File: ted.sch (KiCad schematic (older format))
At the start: 20 parts, among them Q1 2SC1815, Q2 2SC1815, U1 MOS_7360_TED, Y1 Crystal

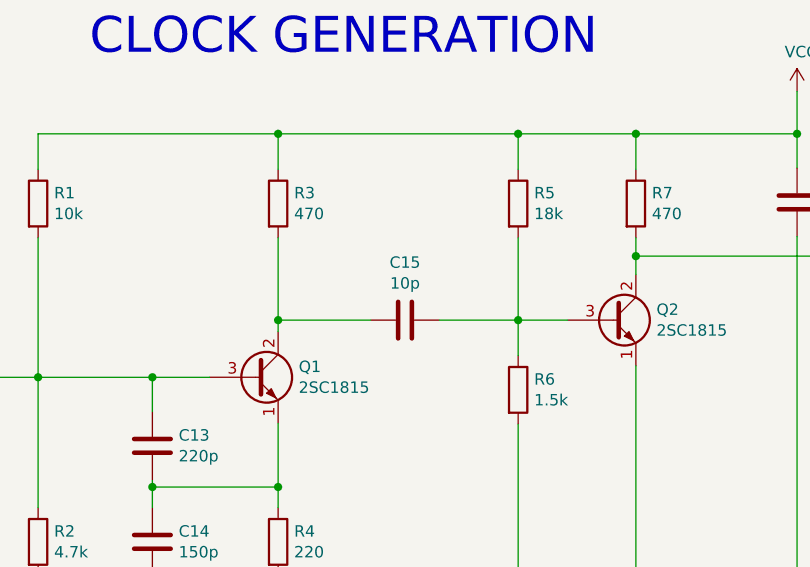
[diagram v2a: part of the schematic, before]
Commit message: C15 -> 10nF
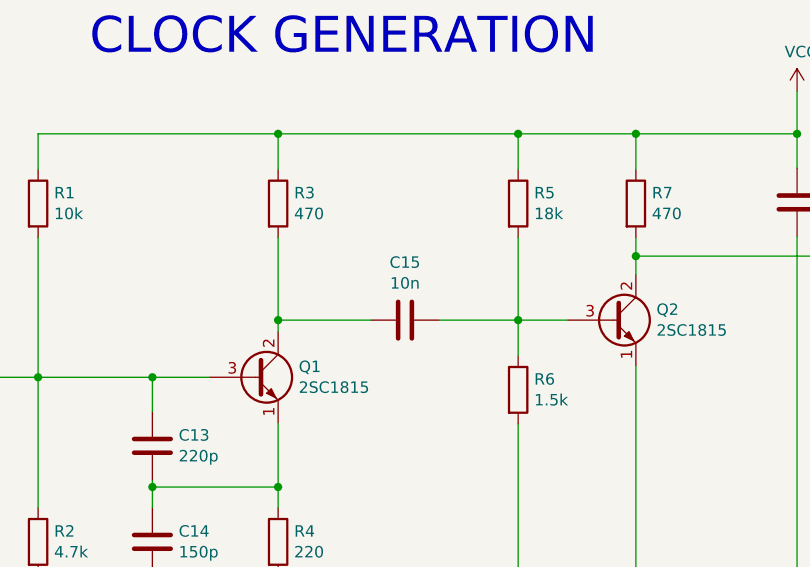
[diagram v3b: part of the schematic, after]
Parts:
- C15: value 10p -> 10n
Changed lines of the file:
@@
 P 3855 3130
 F 0 "C15" V 3603 3130 50  0000 C CNN
-F 1 "10p" V 3694 3130 50  0000 C CNN
+F 1 "10n" V 3694 3130 50  0000 C CNN
 F 2 "Capacitor_THT:C_Disc_D8.0mm_W2.5mm_P5.00mm" H 3893 2980 50  0001 C CNN
 F 3 "~" H 3855 3130 50  0001 C CNN

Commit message: Make most ICs HCT
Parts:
- Q1, Q2: MouserPN (none) -> 610-2SC1815-GR
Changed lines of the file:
@@
 F 2 "Package_TO_SOT_THT:TO-92_Inline_Wide" H 3400 3305 50  0001 L CIN
 F 3 "https://media.digikey.com/pdf/Data%20Sheets/Toshiba%20PDFs/2SC1815.pdf" H 3200 3380 50  0001 L CNN
+F 4 "610-2SC1815-GR" H 3200 3380 50  0001 C CNN "MouserPN"
 	1    3200 3380
 	1    0    0    -1
@@
 F 2 "Package_TO_SOT_THT:TO-92_Inline_Wide" H 4965 3055 50  0001 L CIN
 F 3 "https://media.digikey.com/pdf/Data%20Sheets/Toshiba%20PDFs/2SC1815.pdf" H 4765 3130 50  0001 L CNN
+F 4 "610-2SC1815-GR" H 4765 3130 50  0001 C CNN "MouserPN"
 	1    4765 3130
 	1    0    0    -1

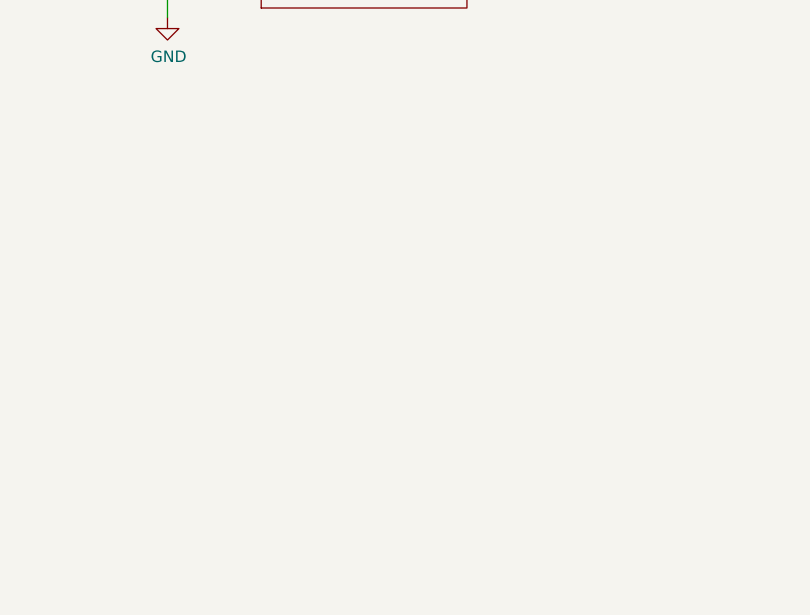
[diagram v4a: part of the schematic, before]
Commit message: Add TED direct audio output header (Experimental)
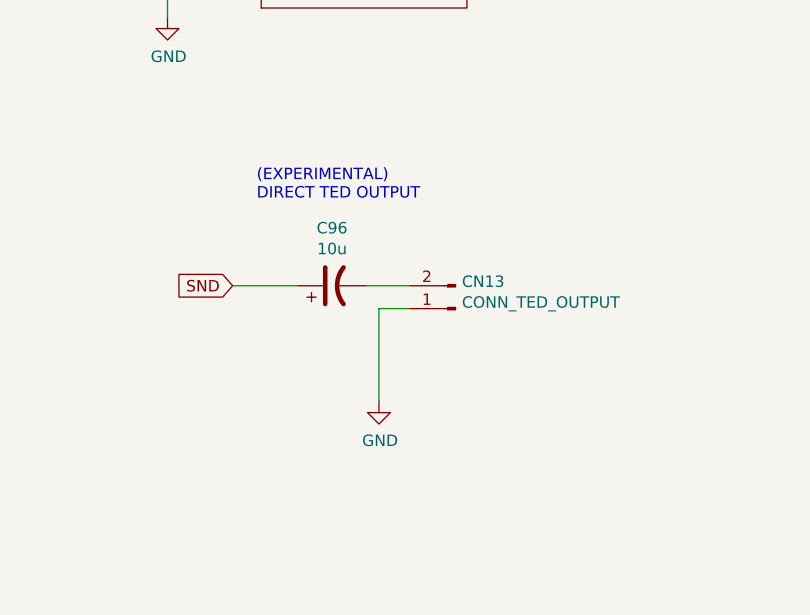
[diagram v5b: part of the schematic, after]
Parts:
- added C96: 10u, Capacitor_THT:CP_Radial_D5.0mm_P2.00mm, symbol Device:CP1
- added CN13: CONN_TED_OUTPUT, Connector_PinHeader_2.54mm:PinHeader_1x02_P2.54mm_Vertical, symbol Connector:Conn_01x02_Male
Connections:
- net GND: now also CN13.1 (Pin_1)
- net SND: now also C96.1
- new net: C96.2, CN13.2 (Pin_2)
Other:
- note added: "(EXPERIMENTAL)\nDIRECT TED OUTPUT"
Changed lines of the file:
@@
 	0    -1   1    0
 $EndComp
+Wire Wire Line
+	8250 5365 8250 5770
+Wire Wire Line
+	8385 5365 8250 5365
+Text Notes 7715 4895 0    50   ~ 0
+(EXPERIMENTAL)\nDIRECT TED OUTPUT
+Wire Wire Line
+	8195 5265 8385 5265
+$Comp
+L Connector:Conn_01x02_Male CN?
+U 1 1 64CE27EC
+P 8585 5365
+AR Path="/64A6E6F3/64CE27EC" Ref="CN?"  Part="1"
+AR Path="/5DE044CB/64CE27EC" Ref="CN13"  Part="1"
+F 0 "CN13" H 8557 5247 50  0000 R CNN
+F 1 "CONN_TED_OUTPUT" H 8557 5338 50  0000 R CNN
+F 2 "Connector_PinHeader_2.54mm:PinHeader_1x02_P2.54mm_Vertical" H 8585 5365 50  0001 C CNN
+F 3 "~" H 8585 5365 50  0001 C CNN
+	1    8585 5365
+	-1   0    0    1
+$EndComp
+$Comp
+L Device:CP1 C?
+U 1 1 64CE27F4
+P 8045 5265
+AR Path="/64A6E6F3/64CE27F4" Ref="C?"  Part="1"
+AR Path="/5DE044CB/64CE27F4" Ref="C96"  Part="1"
+F 0 "C96" V 8297 5265 50  0000 C CNN
+F 1 "10u" V 8206 5265 50  0000 C CNN
+F 2 "Capacitor_THT:CP_Radial_D5.0mm_P2.00mm" H 8045 5265 50  0001 C CNN
+F 3 "~" H 8045 5265 50  0001 C CNN
+F 4 "710-860010472002" H 8045 5265 50  0001 C CNN "MouserPN"
+F 5 "10u" H 8045 5265 50  0001 C CNN "Value"
+	1    8045 5265
+	0    -1   -1   0
+$EndComp
+Text GLabel 7610 5265 0    50   Input ~ 0
+SND
+Wire Wire Line
+	7610 5265 7895 5265
 Wire Bus Line
 	6865 885  6865 1650
@@
 Wire Bus Line
 	9505 885  9505 2650
+$Comp
+L power:GND #PWR?
+U 1 1 64CF4BA6
+P 8250 5770
+AR Path="/5E4A81E1/64CF4BA6" Ref="#PWR?"  Part="1"
+AR Path="/5DE044CB/64CF4BA6" Ref="#PWR?"  Part="1"
+F 0 "#PWR?" H 8250 5520 50  0001 C CNN
+F 1 "GND" H 8255 5597 50  0000 C CNN
+F 2 "" H 8250 5770 50  0001 C CNN
+F 3 "" H 8250 5770 50  0001 C CNN
+	1    8250 5770
+	1    0    0    -1
+$EndComp
 $EndSCHEMATC

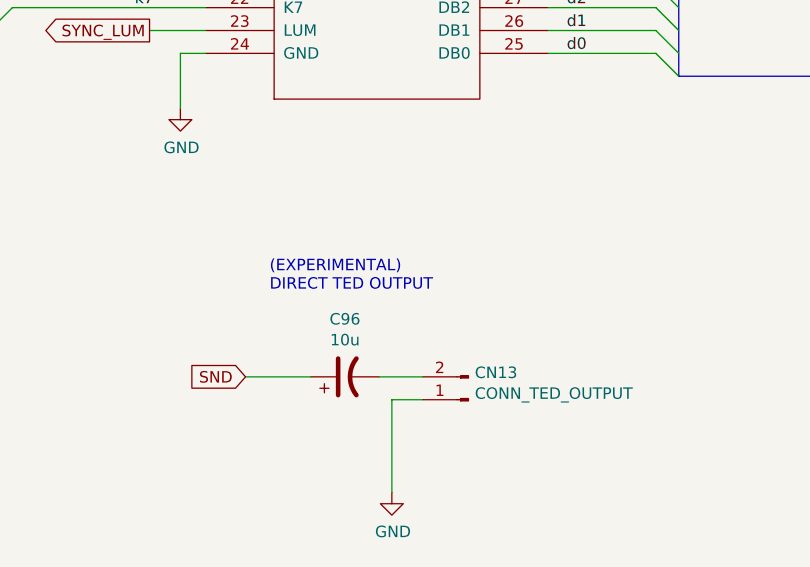
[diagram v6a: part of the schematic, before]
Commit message: Update schematics PDF
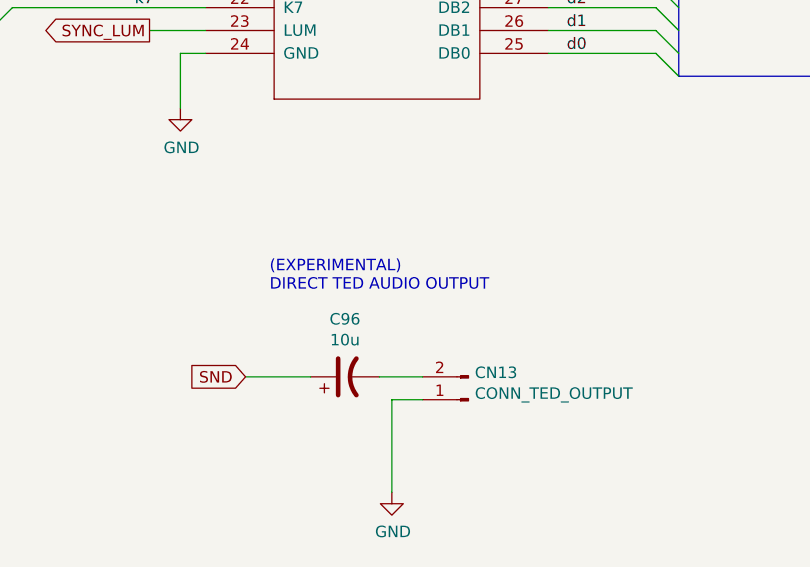
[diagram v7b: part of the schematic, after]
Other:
- note added: "(EXPERIMENTAL)\nDIRECT TED AUDIO OUTPUT"
- note removed: "(EXPERIMENTAL)\nDIRECT TED OUTPUT"
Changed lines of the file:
@@
 Title "LittleSixteen"
 Date "2020-01-03"
-Rev "3git"
+Rev "4git"
 Comp "SukkoPera"
 Comment1 "Licensed under CC BY-NC-SA 4.0"
@@
 	8385 5365 8250 5365
 Text Notes 7715 4895 0    50   ~ 0
-(EXPERIMENTAL)\nDIRECT TED OUTPUT
+(EXPERIMENTAL)\nDIRECT TED AUDIO OUTPUT
 Wire Wire Line
 	8195 5265 8385 5265

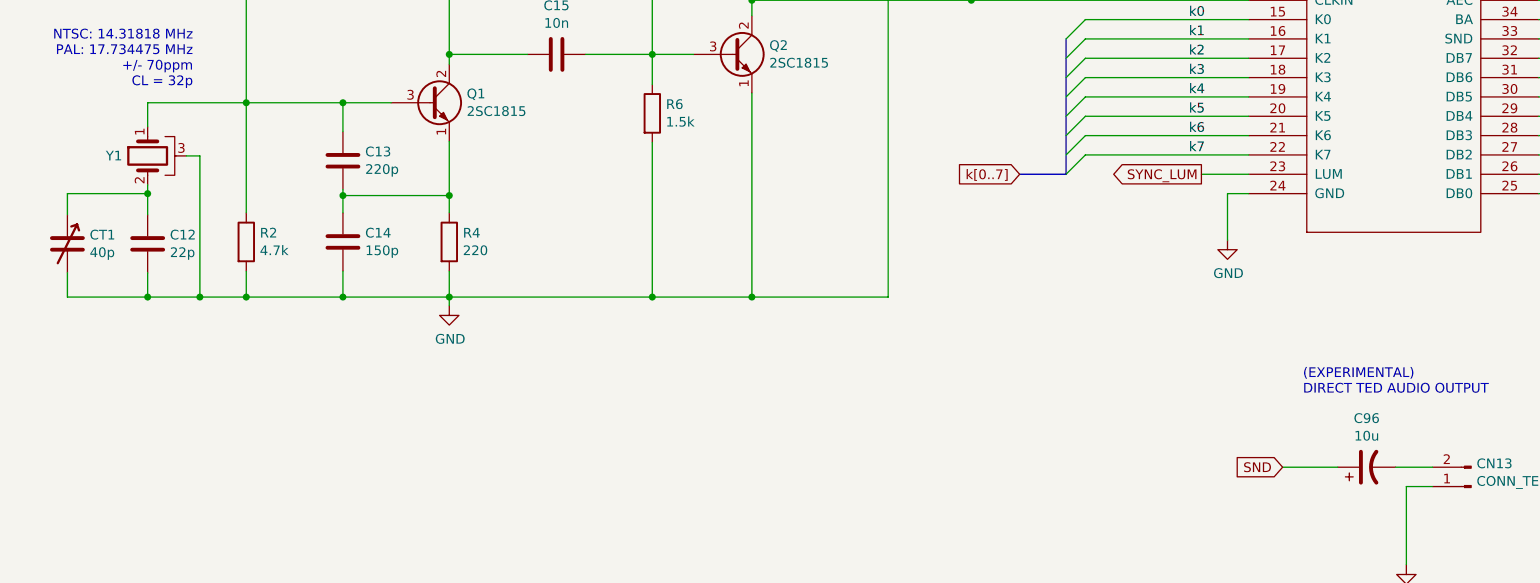
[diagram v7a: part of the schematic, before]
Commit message: Rationalize BOM There should be no significant changes on both schematics on PCB, just some values and something on the silkscreen
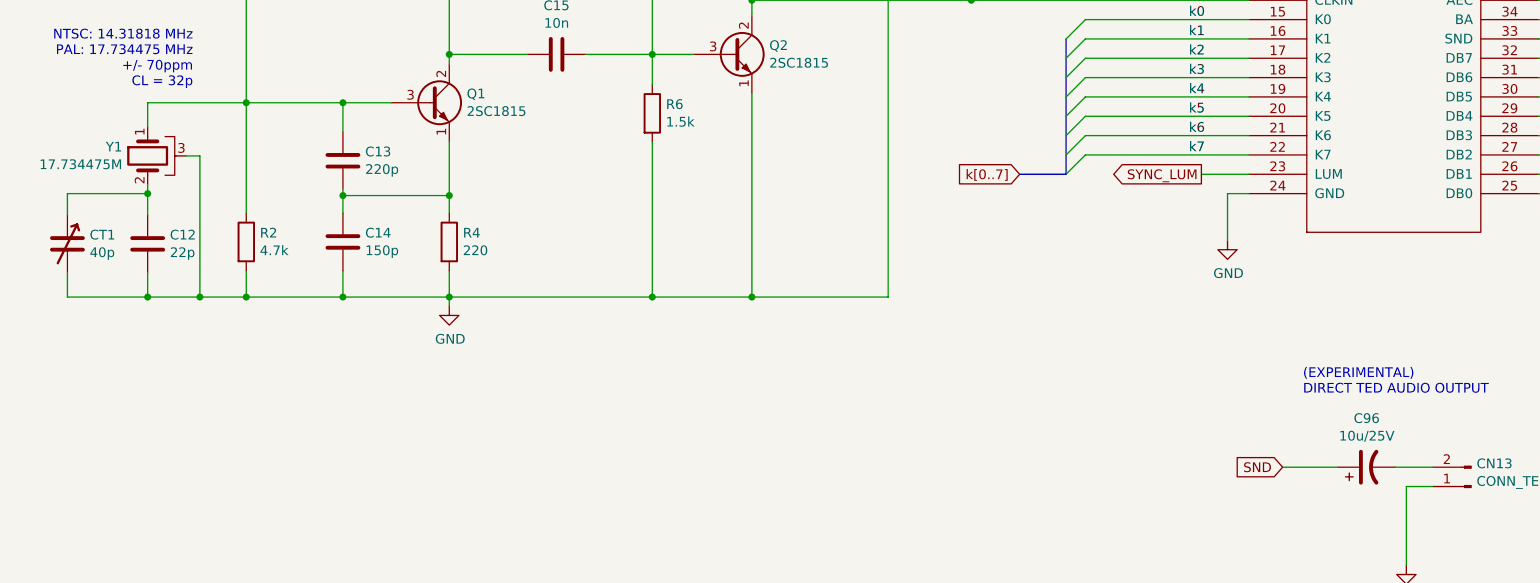
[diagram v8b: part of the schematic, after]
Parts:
- C21: MouserPN (none) -> 810-FG28X7R1H104KNT0
- C32: MouserPN (none) -> 810-FG28C0G2A101JNT6
- C96: value 10u -> 10u/25V
- Y1: value Crystal -> 17.734475M; Notes (none) -> Use 14.31818M for NTSC, +/- 70ppm, CL = 32p
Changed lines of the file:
@@
 F 2 "Capacitor_THT:C_Disc_D8.0mm_W2.5mm_P5.00mm" H 6518 6935 50  0001 C CNN
 F 3 "~" H 6480 7085 50  0001 C CNN
+F 4 "810-FG28X7R1H104KNT0" H 6480 7085 50  0001 C CNN "MouserPN"
 	1    6480 7085
 	1    0    0    -1
@@
 F 2 "Capacitor_THT:C_Disc_D8.0mm_W2.5mm_P5.00mm" H 5608 2465 50  0001 C CNN
 F 3 "~" H 5570 2615 50  0001 C CNN
+F 4 "810-FG28C0G2A101JNT6" H 5570 2615 50  0001 C CNN "MouserPN"
 	1    5570 2615
 	1    0    0    -1
@@
 U 1 1 5E276D96
 P 1740 3655
-F 0 "Y1" V 1740 3786 50  0000 L CNN
-F 1 "Crystal" V 1695 3786 50  0001 L CNN
+F 0 "Y1" V 1694 3786 50  0000 L CNN
+F 1 "17.734475M" V 1785 3786 50  0000 L CNN
 F 2 "Crystal:Crystal_HC49-U_Horizontal_1EP_style2" H 1740 3655 50  0001 C CNN
 F 3 "~" H 1740 3655 50  0001 C CNN
+F 4 "Use 14.31818M for NTSC, +/- 70ppm, CL = 32p" H 1740 3655 50  0001 C CNN "Notes"
 	1    1740 3655
 	0    -1   1    0
@@
 AR Path="/5DE044CB/64CE27F4" Ref="C96"  Part="1"
 F 0 "C96" V 8297 5265 50  0000 C CNN
-F 1 "10u" V 8206 5265 50  0000 C CNN
+F 1 "10u/25V" V 8206 5265 50  0000 C CNN
 F 2 "Capacitor_THT:CP_Radial_D5.0mm_P2.00mm" H 8045 5265 50  0001 C CNN
 F 3 "~" H 8045 5265 50  0001 C CNN
